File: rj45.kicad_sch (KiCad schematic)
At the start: 4 parts, among them J4 RJ45-Ethernet

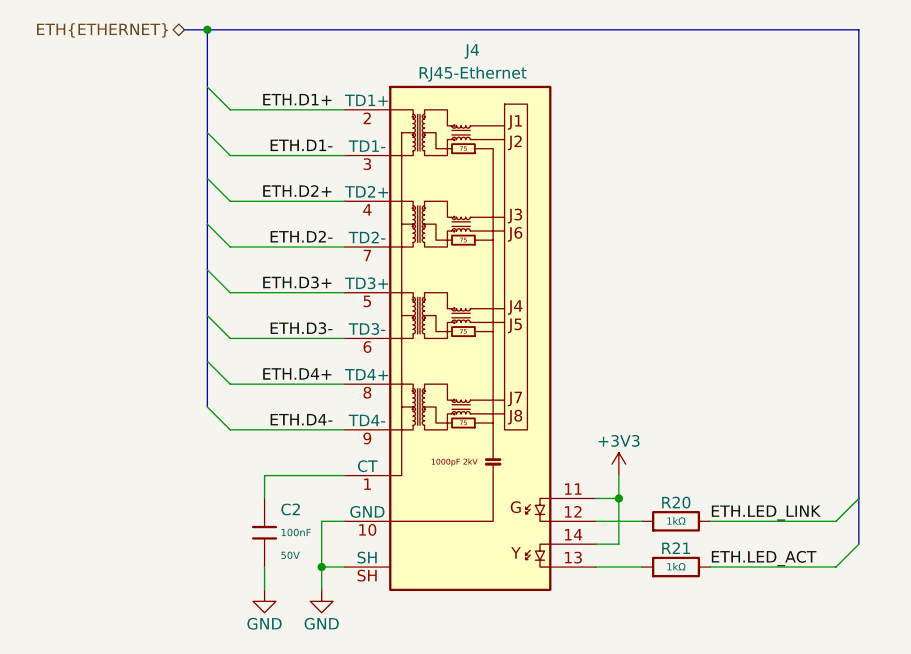
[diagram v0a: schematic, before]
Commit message: [#1] WIP: Change components to ones from the global library, refactor schematic
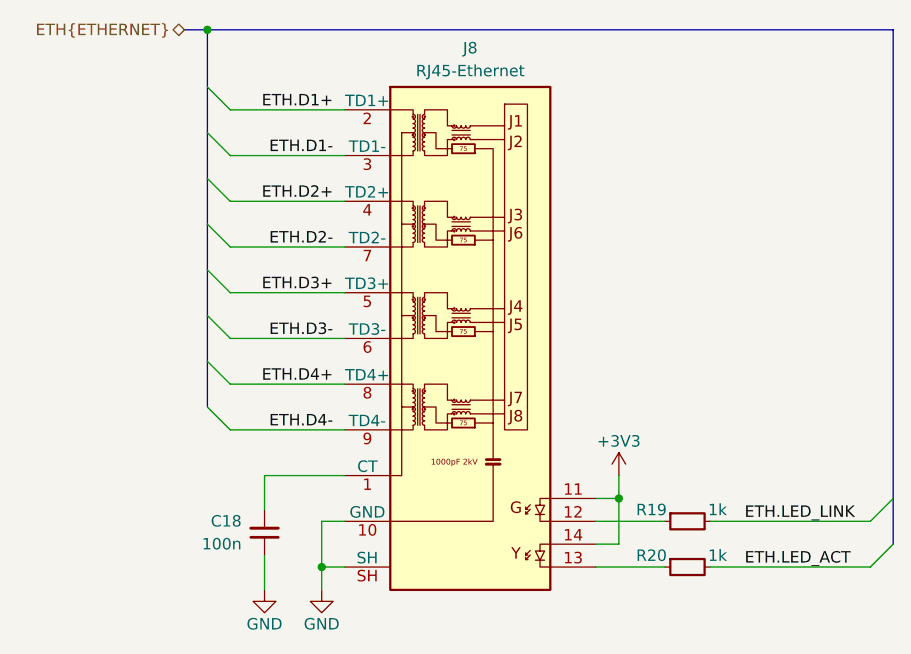
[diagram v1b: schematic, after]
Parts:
- removed C2: 100nF, PCM_JLCPCB:C_0402, symbol PCM_JLCPCB-Capacitors:0402,100nF,(2)
- removed J4: RJ45-Ethernet, lib:RJ45-HC612601A-M893-A, symbol connectors:RJ45-HC612601A-M893-A
- removed R20, R21: 1kΩ, PCM_JLCPCB:R_0402, symbol PCM_JLCPCB-Resistors:0402,1kΩ
- added C18: C-100n-0402, DW-footprints:C_0402_1005Metric, symbol DW-capacitors:C-100n-0402
- added J8: RJ45-Ethernet, DW-footprints:RJ45_HC612601A-M893-A, symbol DW-connectors:RJ45_HC612601A-M893-A
- added R19, R20: R-1k-0402, DW-footprints:R_0402_1005Metric, symbol DW-resistors:R-1k-0402
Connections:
- net +3V3: now also J8.11, J8.14
- net ETH.D1+: now also J8.2 (TD1+)
- net ETH.D1-: now also J8.3 (TD1-)
- net ETH.D2+: now also J8.4 (TD2+)
- net ETH.D2-: now also J8.7 (TD2-)
- net ETH.D3+: now also J8.5 (TD3+)
- net ETH.D3-: now also J8.6 (TD3-)
- net ETH.D4+: now also J8.8 (TD4+)
- net ETH.D4-: now also J8.9 (TD4-)
- net ETH.LED_ACT: now also R20.2
- net ETH.LED_LINK: now also R19.2
- net GND: now also C18.1, J8.10 (GND), J8.SH
- new net: J8.13, R20.1
- new net: J8.12, R19.1
- new net: C18.2, J8.1 (CT)
